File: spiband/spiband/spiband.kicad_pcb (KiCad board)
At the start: 2 copper layers, 44 parts, among them J1 RJ45_Shielded, J2 Conn_01x06, J3 Conn_01x06, J4 Conn_01x06, U1 MAX3485, U10 SN74LVC1T45DBV, U2 MAX3485, U3 MAX3485, U4 MAX3232, U5 LM78M05_TO220, U6 TLV70018_SOT353, U7 74LS153, U8 SN74LVC1T45DBV, U9 SN74LVC1T45DBV

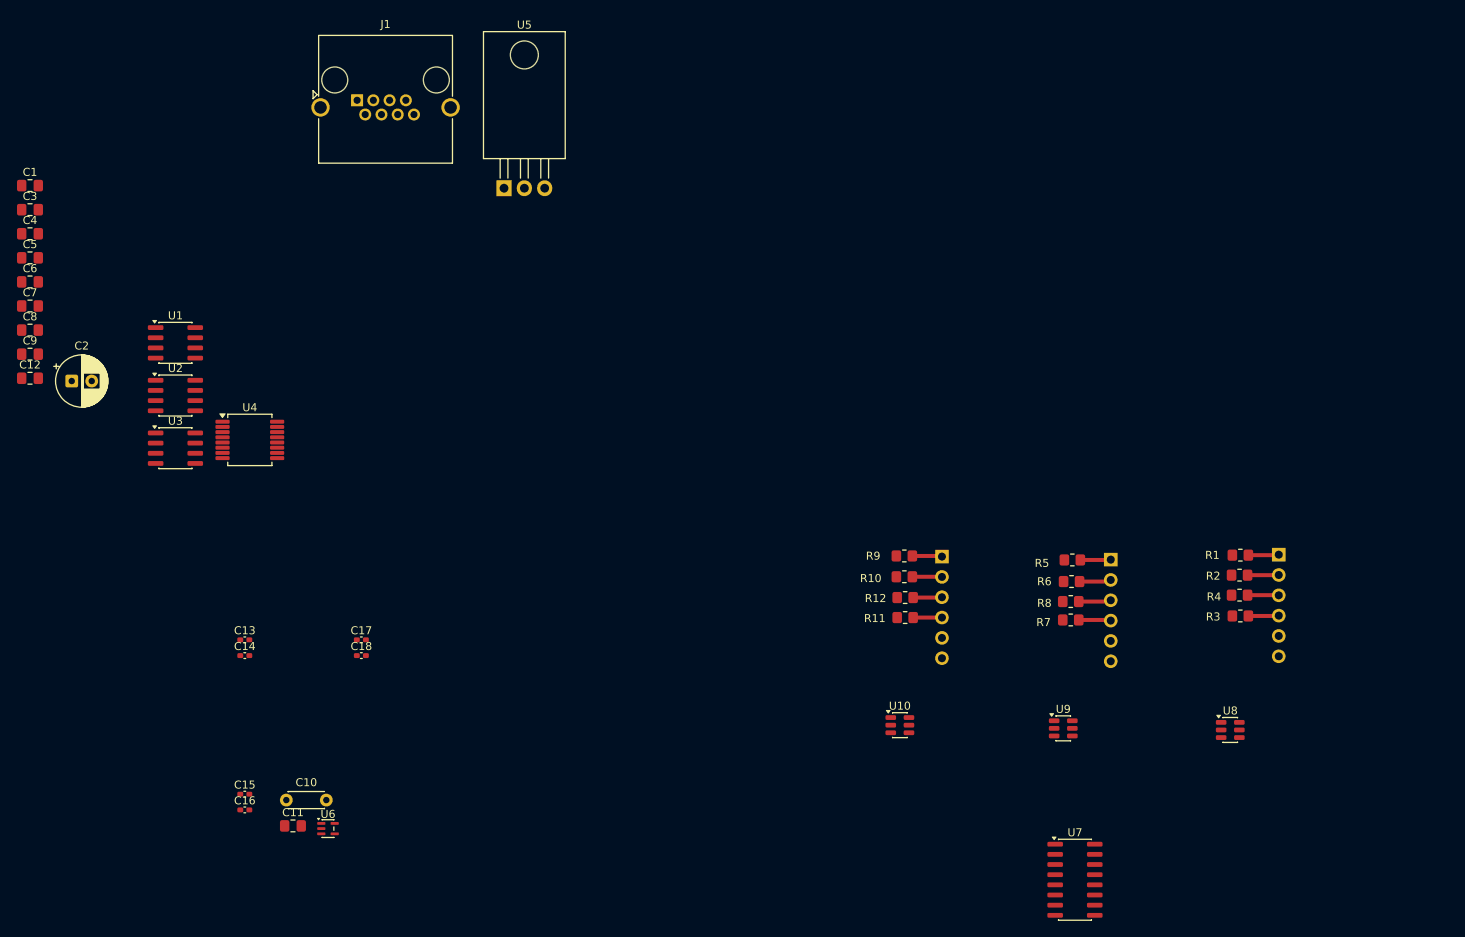
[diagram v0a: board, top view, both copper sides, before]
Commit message: Changed to 3.3v supply voltage.
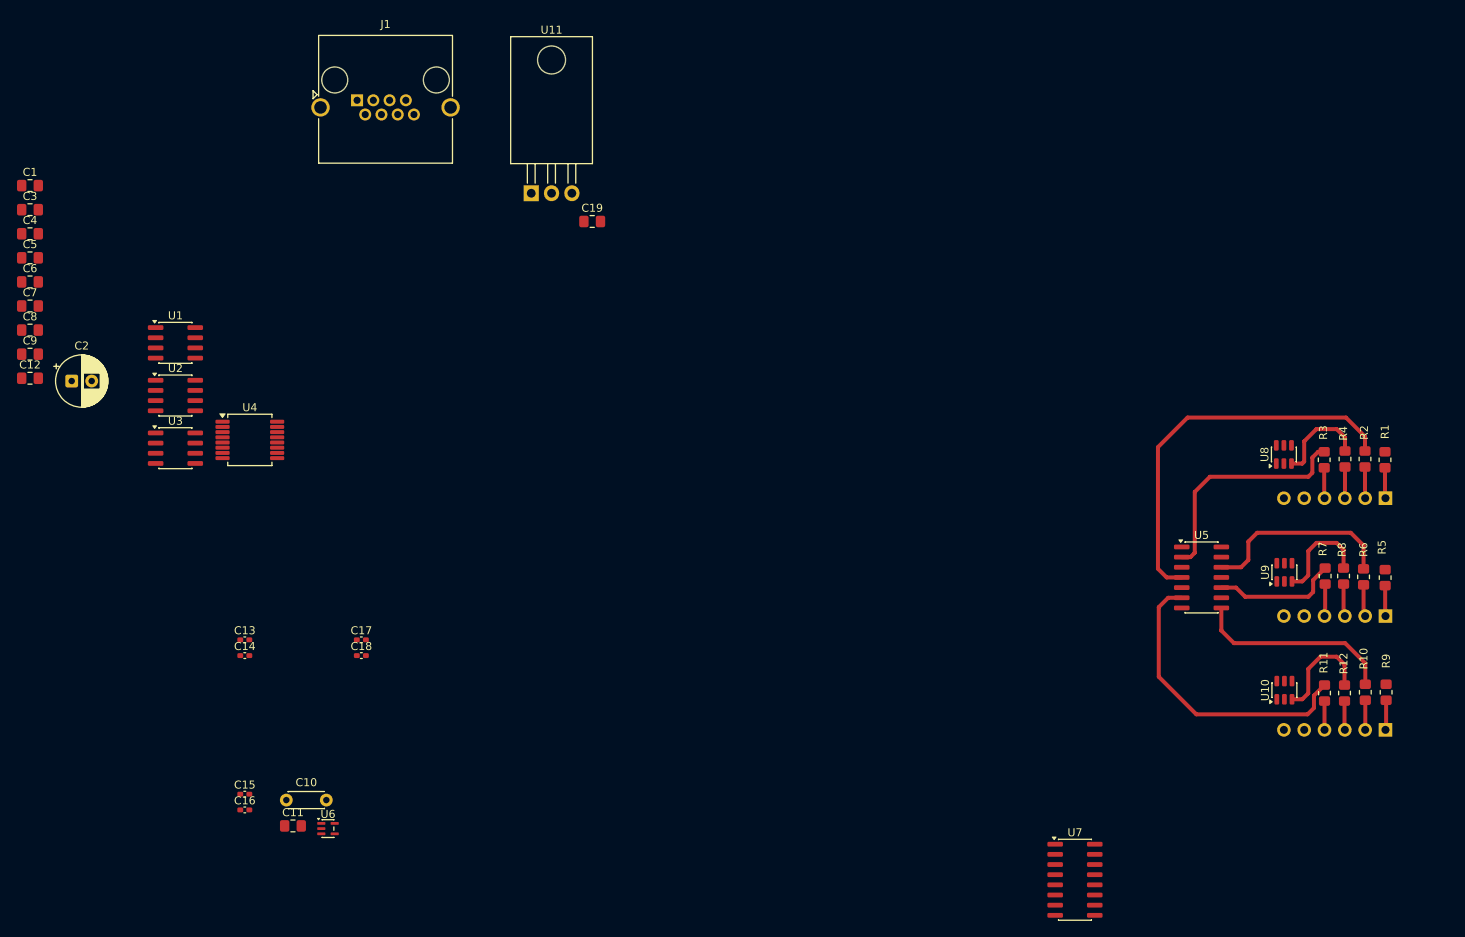
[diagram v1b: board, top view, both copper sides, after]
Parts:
- added C19: 100n, Capacitor_SMD:C_0805_2012Metric_Pad1.18x1.45mm_HandSolder, F.Cu at (106.6, 59.4)
- added U11: LM1086CT-3.3, Package_TO_SOT_THT:TO-220-3_Horizontal_TabDown, F.Cu at (99.0, 55.9)
- U5: value LM78M05_TO220 -> 74HC04; footprint Package_TO_SOT_THT:TO-220-3_Horizontal_TabDown -> Package_SO:SOIC-14_3.9x8.7mm_P1.27mm
- U7: value 74LS153 -> 74HC153
- moved U5 99.8 mm to (182.7, 103.9)
- moved R9 62.6 mm to (205.8, 118.2), turned to -90 degrees
- moved J4 59.5 mm to (205.7, 122.9), turned to 90 degrees
- moved R10 59.4 mm to (203.2, 118.2), turned to -90 degrees
- moved R12 56.2 mm to (200.6, 118.3), turned to -90 degrees
- moved R11 53.3 mm to (198.1, 118.3), turned to -90 degrees
- moved U10 48.3 mm to (193.1, 118.0), turned to 90 degrees
- moved R5 39.2 mm to (205.7, 103.9), turned to -90 degrees
- moved R6 36.5 mm to (203.0, 103.8), turned to -90 degrees
- moved U8 35.1 mm to (193.0, 88.5), turned to 90 degrees
- moved J3 35.1 mm to (205.7, 108.7), turned to 90 degrees
- moved R8 34.2 mm to (200.5, 103.7), turned to -90 degrees
- moved U9 33.8 mm to (193.1, 103.2), turned to 90 degrees
- moved R7 32.3 mm to (198.2, 103.7), turned to -90 degrees
- moved R3 22.2 mm to (198.1, 89.2), turned to -90 degrees
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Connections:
- C10 pad 1: 5v -> 3.3v
- C12 pad 1: 5v -> 3.3v
- C13 pad 1: 5v -> 3.3v
- C15 pad 1: 5v -> 3.3v
- C17 pad 1: 5v -> 3.3v
- C2 pad 1: 5v -> 3.3v
- C3 pad 1: 5v -> 3.3v
- C4 pad 1: 5v -> 3.3v
- C5 pad 1: 5v -> 3.3v
- R10 pad 1: IN2 -> /Channel2/SPI_OUT
- R11 pad 1: SPI_CLK -> /Channel2/SPI_CLK
- R2 pad 1: IN0 -> /Channel0/SPI_OUT
- R3 pad 1: SPI_CLK -> /Channel0/SPI_CLK
- R6 pad 1: IN1 -> /Channel1/SPI_OUT
- R7 pad 1: SPI_CLK -> /Channel1/SPI_CLK
- U1 pad 1: SPI_CLK -> INV_CLK
- U1 pad 8: 5v -> 3.3v
- U10 pad 4: SPI_OUT -> IN2
- U10 pad 6: 5v -> 3.3v
- U2 pad 2: 5v -> 3.3v
- U2 pad 3: 5v -> 3.3v
- U2 pad 8: 5v -> 3.3v
- U3 pad 1: SPI_OUT -> INV_OUT
- U3 pad 8: 5v -> 3.3v
- U4 pad 16: unconnected-(U4-VCC-Pad16) -> 3.3v
- U5 pad 1: 9v -> INV_CLK
- U5 pad 2: unconnected-(U5-GND-Pad2) -> /Channel0/SPI_CLK
- U5 pad 3: 5v -> INV_OUT
- U6 pad 1: 5v -> 3.3v
- U6 pad 3: 5v -> 3.3v
- U7 pad 13: 5v -> 3.3v
- U7 pad 16: 5v -> 3.3v
- U8 pad 4: SPI_OUT -> IN0
- U8 pad 6: 5v -> 3.3v
- U9 pad 4: SPI_OUT -> IN1
- U9 pad 6: 5v -> 3.3v
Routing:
- net /Channel0/SPI_OUT: track 0.00 -> 48.8 mm
- net /Channel2/SPI_CLK: track 0.00 -> 37.1 mm
- net /Channel0/SPI_CLK: track 0.00 -> 28.8 mm
- net /Channel2/SPI_OUT: track 0.00 -> 25.2 mm
- net /Channel1/SPI_OUT: track 0.00 -> 24.5 mm
- net /Channel1/SPI_CLK: track 0.00 -> 15.8 mm
- net Net-(U10-A): track 0.00 -> 13.5 mm
- net Net-(U9-A): track 0.00 -> 12.9 mm
- net Net-(U8-A): track 0.00 -> 12.1 mm

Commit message: Finalized SPI interface PCB
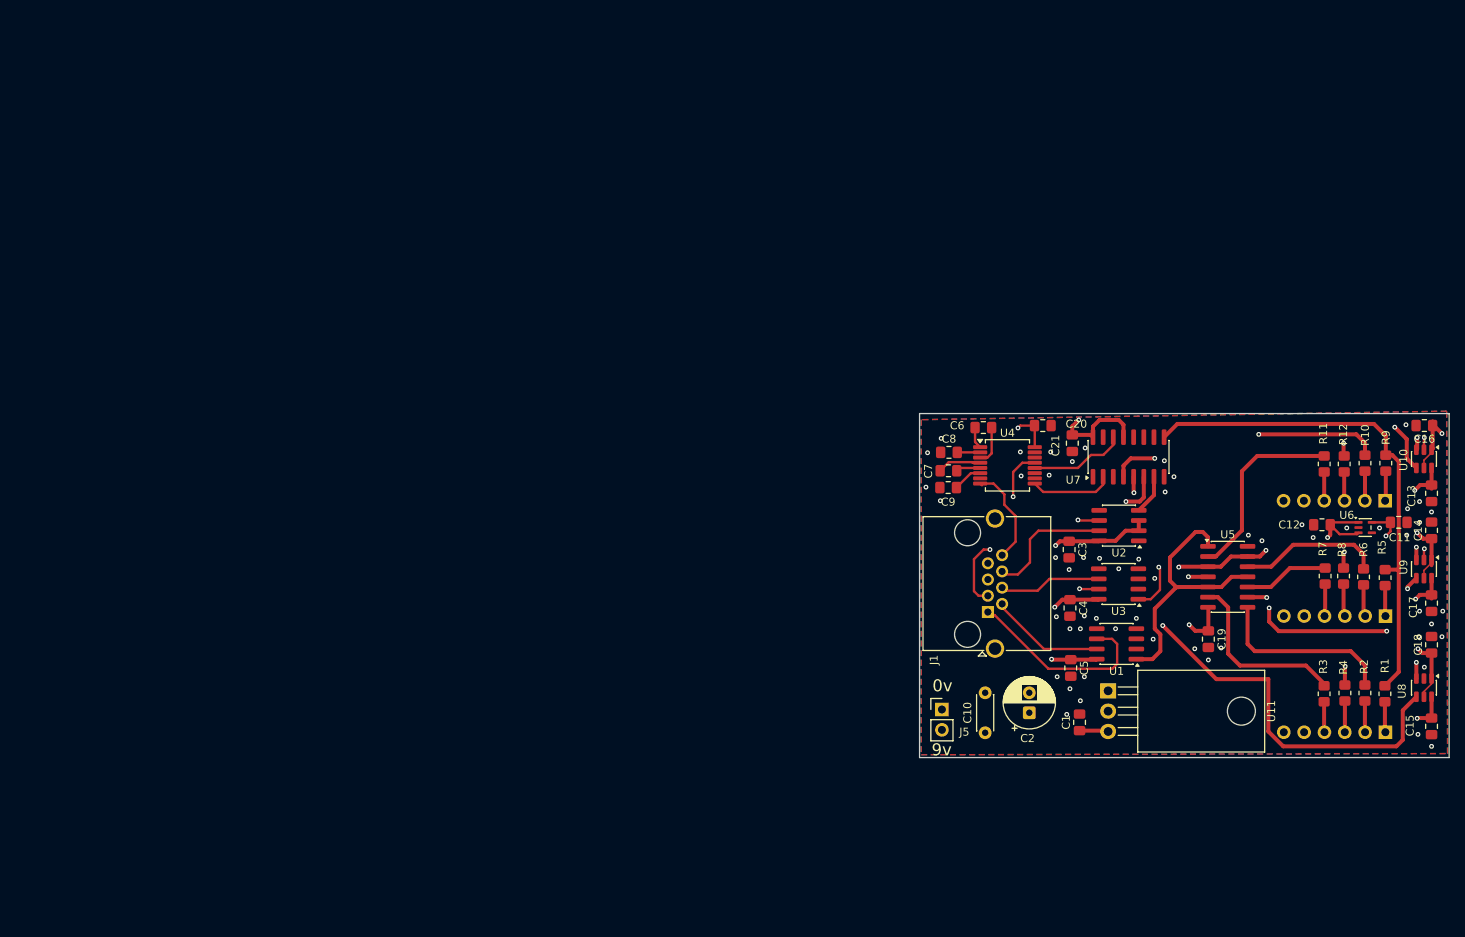
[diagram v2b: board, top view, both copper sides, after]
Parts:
- added C20: 100n, Capacitor_SMD:C_0805_2012Metric_Pad1.18x1.45mm_HandSolder, F.Cu at (162.9, 84.9)
- added C21: 100n, Capacitor_SMD:C_0805_2012Metric_Pad1.18x1.45mm_HandSolder, F.Cu at (166.6, 87.1)
- added J5: Conn_01x02, Connector_PinHeader_2.54mm:PinHeader_1x02_P2.54mm_Vertical, F.Cu at (150.3, 120.4)
- C13, C14, C15, C16, C17, C18: footprint Capacitor_SMD:C_0402_1005Metric_Pad0.74x0.62mm_HandSolder -> Capacitor_SMD:C_0805_2012Metric_Pad1.18x1.45mm_HandSolder
- moved C12 162.5 mm to (197.8, 97.3), turned to 180 degrees
- moved C16 155.1 mm to (210.6, 84.9), turned to 180 degrees
- moved C13 149.5 mm to (211.5, 93.4), turned to -90 degrees
- moved C14 149.2 mm to (211.5, 98.0), turned to 90 degrees
- moved C15 148.6 mm to (211.5, 122.5), turned to -90 degrees
- moved C1 147.4 mm to (167.5, 122.0), turned to 90 degrees
- moved C11 143.3 mm to (207.4, 97.0)
- moved C5 139.8 mm to (166.4, 115.2), turned to -90 degrees
- moved C4 138.2 mm to (166.3, 107.7), turned to -90 degrees
- moved C3 136.7 mm to (166.2, 100.4), turned to -90 degrees
- moved U6 135.0 mm to (203.2, 97.7)
- moved C17 133.9 mm to (211.5, 107.1), turned to -90 degrees
- moved C18 133.8 mm to (211.5, 112.3), turned to 90 degrees
- moved C2 126.7 mm to (161.2, 120.8), turned to 90 degrees
- moved U1 123.5 mm to (172.1, 112.2), turned to 180 degrees
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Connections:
- J1 pad SH: unconnected-(J1-PadSH) -> GND
- U5 pad 2: /Channel0/SPI_CLK -> /Channel2/SPI_CLK
- U5 pad 4: /Channel0/SPI_OUT -> /Channel2/SPI_OUT
- U5 pad 6: /Channel2/SPI_CLK -> /Channel0/SPI_CLK
- U5 pad 8: /Channel2/SPI_OUT -> /Channel0/SPI_OUT
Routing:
- net 3.3v: track 0.00 -> 71.1 mm, vias 0 -> 10
- net IN0: track 0.00 -> 69.2 mm, vias 0 -> 2
- net CS: track 0.00 -> 63.9 mm
- net IN1: track 0.00 -> 58.1 mm, vias 0 -> 4
- net IN2: track 0.00 -> 43.5 mm, vias 0 -> 2
- net INV_CLK: track 0.00 -> 33.8 mm
- net INV_OUT: track 0.00 -> 28.7 mm, vias 0 -> 4
- net 1.8v: track 0.00 -> 28.4 mm, vias 0 -> 4
- net /Channel0/SPI_OUT: track 48.8 -> 22.8 mm
- net Net-(U4-R1IN): track 0.00 -> 26.0 mm, vias 0 -> 1
- net Net-(U3-B): track 0.00 -> 24.5 mm, vias 0 -> 1
- net Net-(U1-A): track 0.00 -> 24.5 mm
- net Net-(U2-A): track 0.00 -> 23.7 mm, vias 0 -> 2
- net Net-(U2-B): track 0.00 -> 16.1 mm
- net Net-(U1-B): track 0.00 -> 14.0 mm
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- added copper zone on In1.Cu, net 1.8v
- added copper zone on In2.Cu, net 3.3v
- added copper zone on In1.Cu, net 9v
- added copper zone on B.Cu, net GND
- added copper zone on F.Cu, net GND
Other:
- board outline added: 66.2 x 43 mm
- copper layers 2 -> 4
- board text added: "0v"
- board text added: "9v"

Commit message: Reworked ADCIO project to use DAC IO.
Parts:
- added J6: Screw_Terminal_01x02, TerminalBlock_Phoenix:TerminalBlock_Phoenix_MKDS-1,5-2_1x02_P5.00mm_Horizontal, F.Cu at (188.4, 88.7)
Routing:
- net /Channel2/SPI_OUT: track 39.2 -> 44.9 mm
- net /Channel2/SPI_CLK: track 24.1 -> 21.3 mm
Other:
- board text added: "3-Channel SPI"

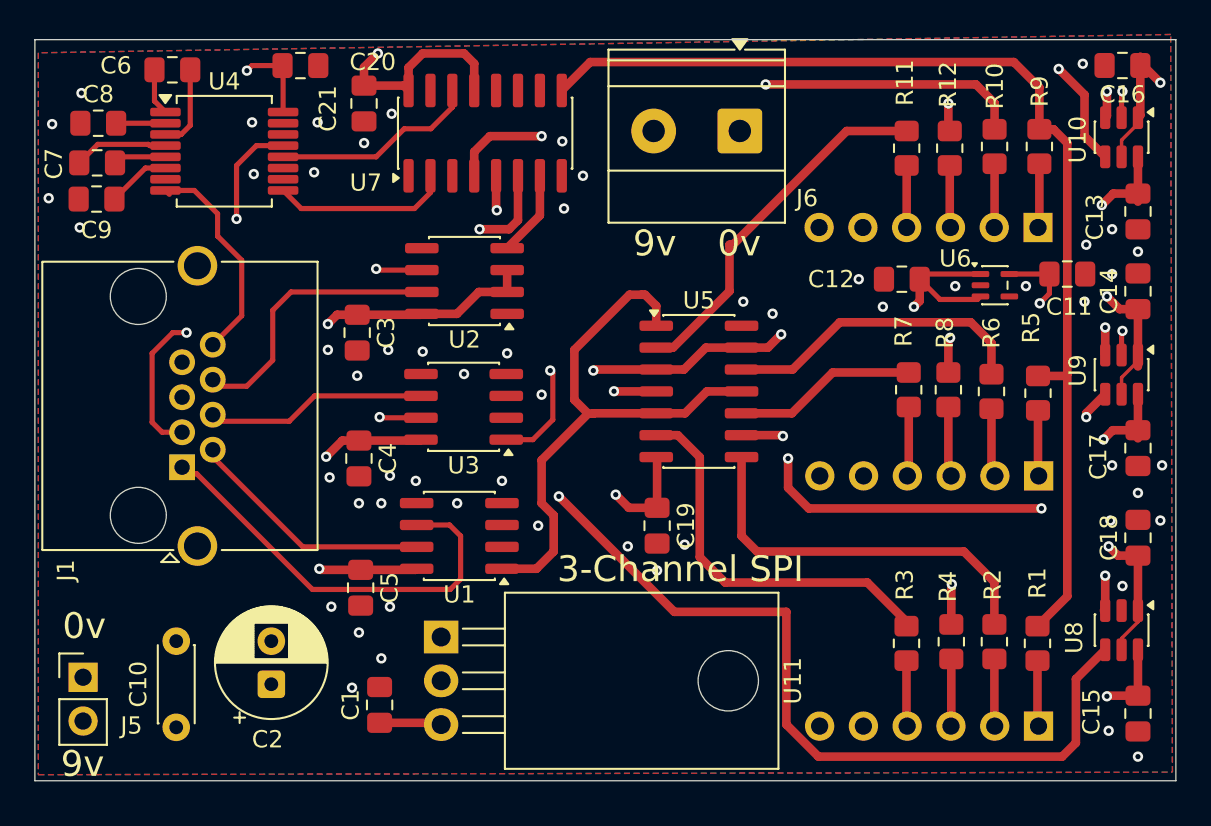
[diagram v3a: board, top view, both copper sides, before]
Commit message: Updated footprints for RJ45 and balun height.
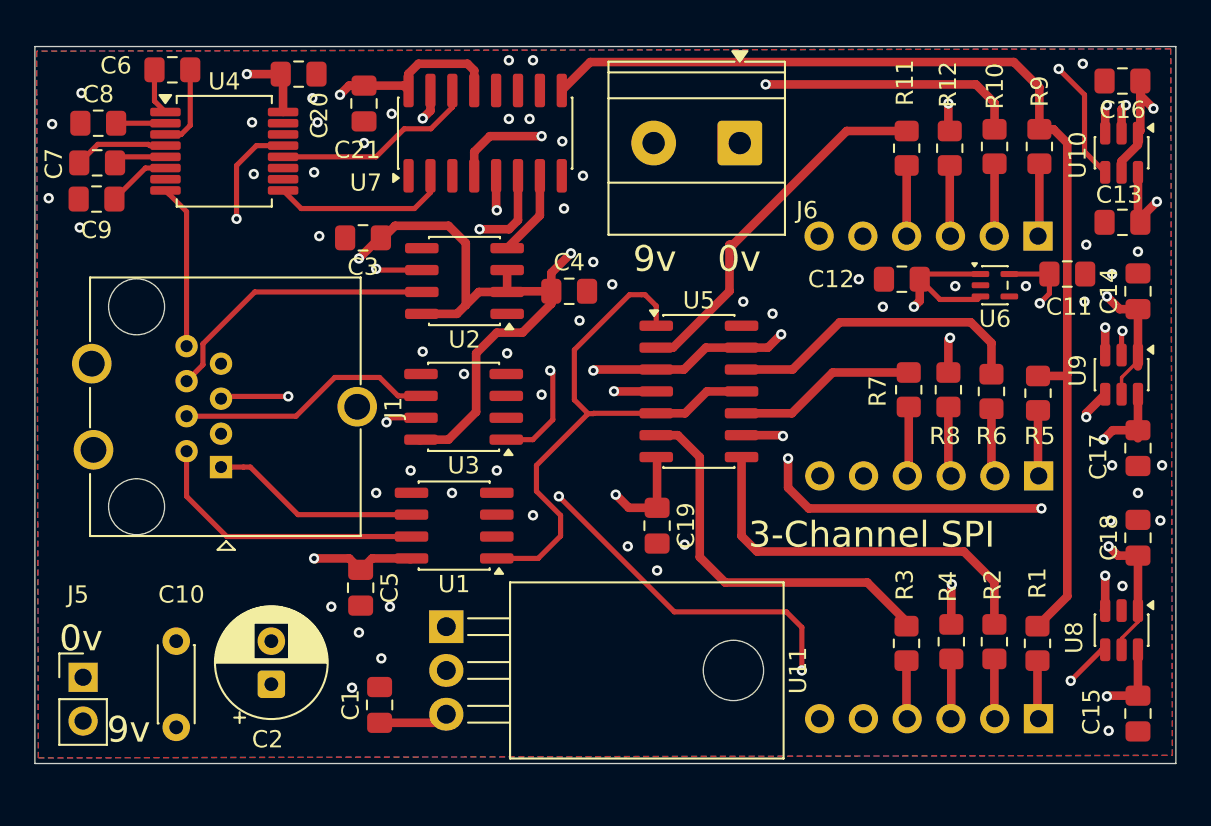
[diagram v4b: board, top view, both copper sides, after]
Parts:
- J1: footprint Connector_RJ:RJ45_Amphenol_RJHSE5380 -> custom:RJ45
- U7: value 74HC153 -> SN74HC153DR1G4
- moved C4 15.6 mm to (178.5, 98.0), turned to 0 degrees
- moved J1 7.12 mm to (157.3, 101.2), turned to -90 degrees
- moved C3 5.51 mm to (166.5, 94.9), turned to 180 degrees
- moved C13 1.10 mm to (210.6, 94.0), turned to 180 degrees
- moved U10 0.90 mm to (210.6, 90.0)
- moved C16 0.90 mm to (210.6, 85.8)
- moved J6 0.70 mm to (188.4, 89.4)
- moved U11 0.67 mm to (171.4, 117.5)
- moved U1 0.67 mm to (171.8, 111.6)
- moved C20 0.51 mm to (162.8, 85.4)
- moved J4 0.50 mm to (205.7, 94.8)
- moved J2 0.43 mm to (205.7, 122.8)
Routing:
- net 3.3v: track 71.1 -> 87.5 mm
- net Net-(U1-A): track 24.5 -> 12.2 mm
- net Net-(U3-B): track 24.5 -> 13.2 mm, vias 1 -> 2
- net Net-(U4-R1IN): track 26.0 -> 15.0 mm
- net IN0: track 69.2 -> 61.0 mm, vias 2 -> 4
- net Net-(U2-A): track 23.7 -> 19.7 mm, vias 2 -> 1
- net Net-(U4-R2IN): track 12.8 -> 9.84 mm
- net Net-(U1-B): track 14.0 -> 16.6 mm
- net Net-(U3-A): track 12.7 -> 15.0 mm
- net GND: track 2.97 -> 4.96 mm, vias 58 -> 60
- net IN2: track 43.5 -> 44.4 mm
- net Net-(J4-Pin_1): track 3.73 -> 4.35 mm
- net 1.8v: track 28.4 -> 27.8 mm
- net Net-(J4-Pin_3): track 3.62 -> 4.17 mm
- net Net-(J4-Pin_2): track 3.71 -> 4.24 mm
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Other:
- board size 66.2 x 43 mm -> 66.2 x 41.6 mm
